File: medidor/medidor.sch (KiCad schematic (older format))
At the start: 26 parts, among them J1 Screw_Terminal_01x02, J2 Conn_01x01_Female, J3 Conn_01x01_Female, J4 Conn_01x06, J5 Screw_Terminal_01x02, U1 LTC1966CMS8PBF, U2 MCP6001U

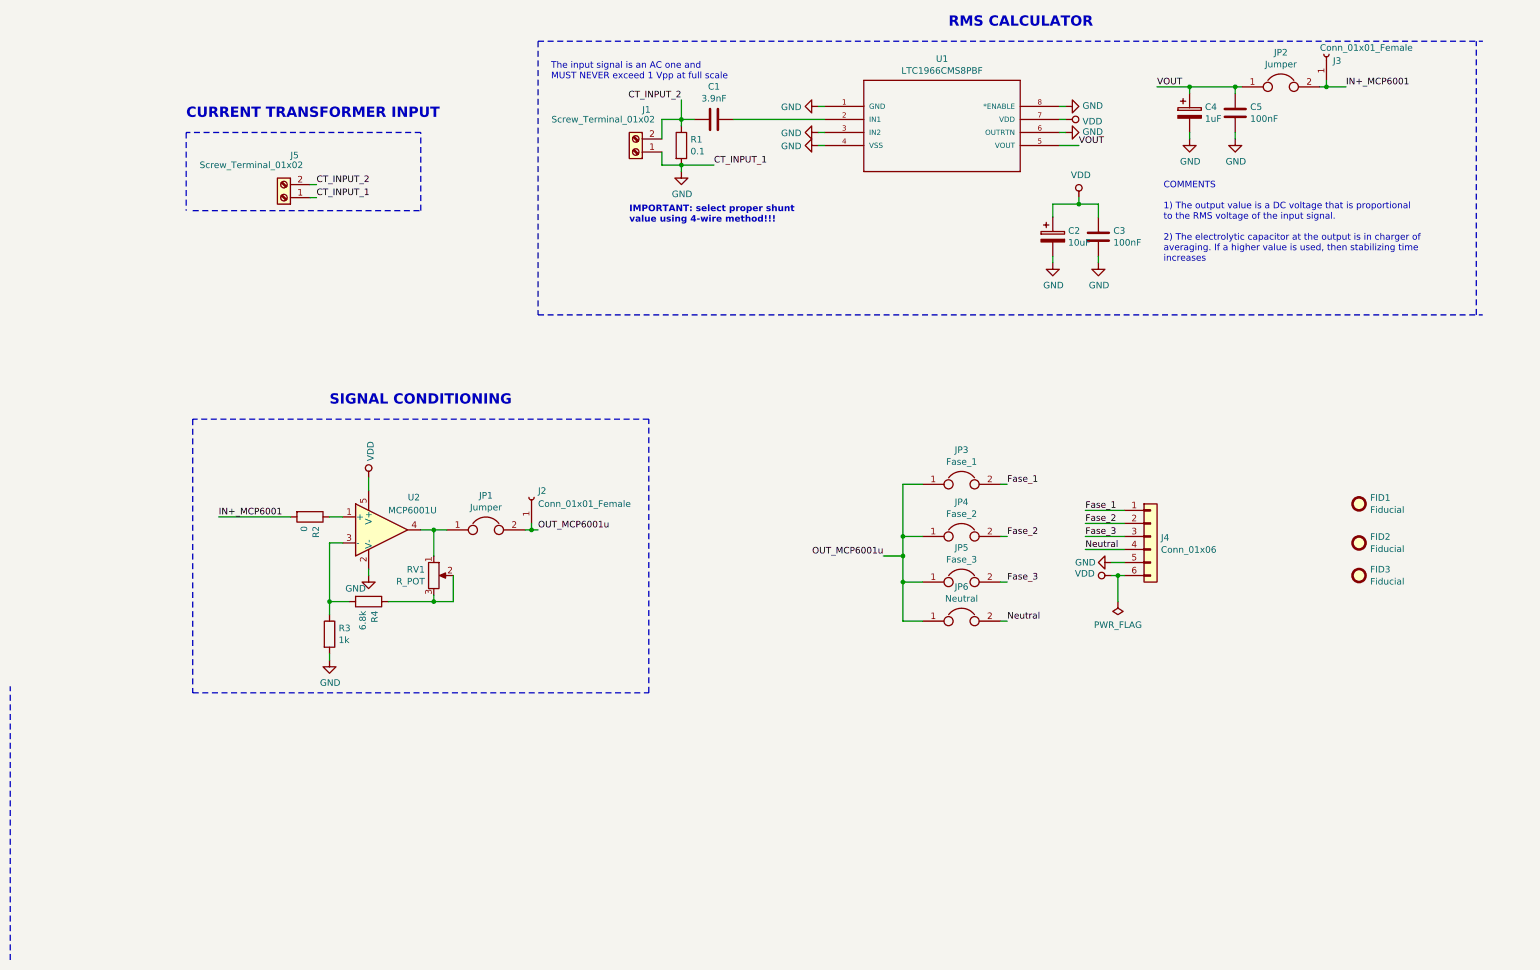
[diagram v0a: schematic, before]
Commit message: Se agregan correcciones sugeridas por el docente y se define la version con shunt TO-220-2
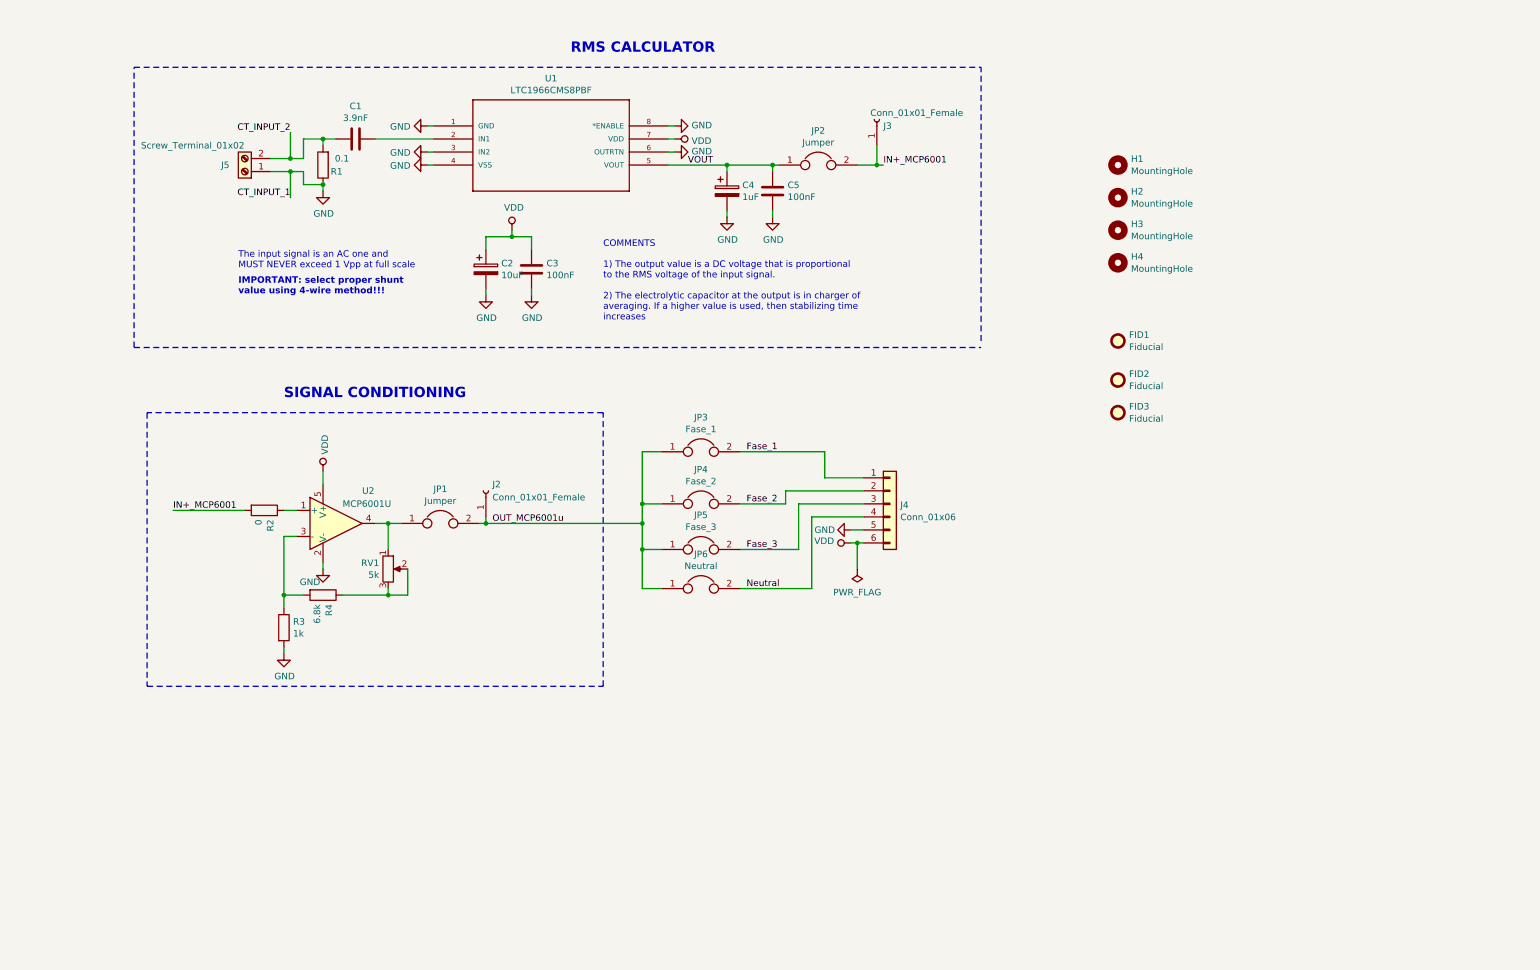
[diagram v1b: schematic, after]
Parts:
- removed J1: Screw_Terminal_01x02, TerminalBlock_MetzConnect:TerminalBlock_MetzConnect_Type703_RT10N02HGLU_1x02_P9.52mm_Horizontal, symbol Connector:Screw_Terminal_01x02
- added H1, H2, H3, H4: MountingHole, MountingHole:MountingHole_4.3mm_M4, symbol Mechanical:MountingHole
- R1: footprint Resistor_THT:R_Axial_Power_L60.0mm_W14.0mm_P71.12mm -> TO_220_2_THT:TO-220-2_Vertical; Digikey_Code (none) -> PWR221T-30-R100F-ND; Model (none) -> PWR221T-30-R100F; Vendor  (none) -> Bourns
- RV1: value R_POT -> 5k; Digikey_Code (none) -> P3V502CT-ND; Model (none) -> EVM-3VSX50B53
- U1: Digikey_Code (none) -> LTC1966CMS8#PBF-ND
- U2: Digikey_Code (none) -> MCP6001UT-I/OTCT-ND; Vendor (none) -> Microchip
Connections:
- net CT_INPUT_2: now also R1.2; no longer R1.1
- net GND: now also R1.1; no longer R1.2
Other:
- note removed: "CURRENT TRANSFORMER INPUT"
- moved on the sheet: C1, C2, C3, C4, C5, FID1, FID2, FID3, J2, J3, J4, J5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
